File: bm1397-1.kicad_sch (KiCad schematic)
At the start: 58 parts, among them IC1 BM1397_mode1, J8 Conn_01x05, U5 MCP1824T-1802E, U6 MCP1824T-0802E, X1 OT322525MJBA4SL

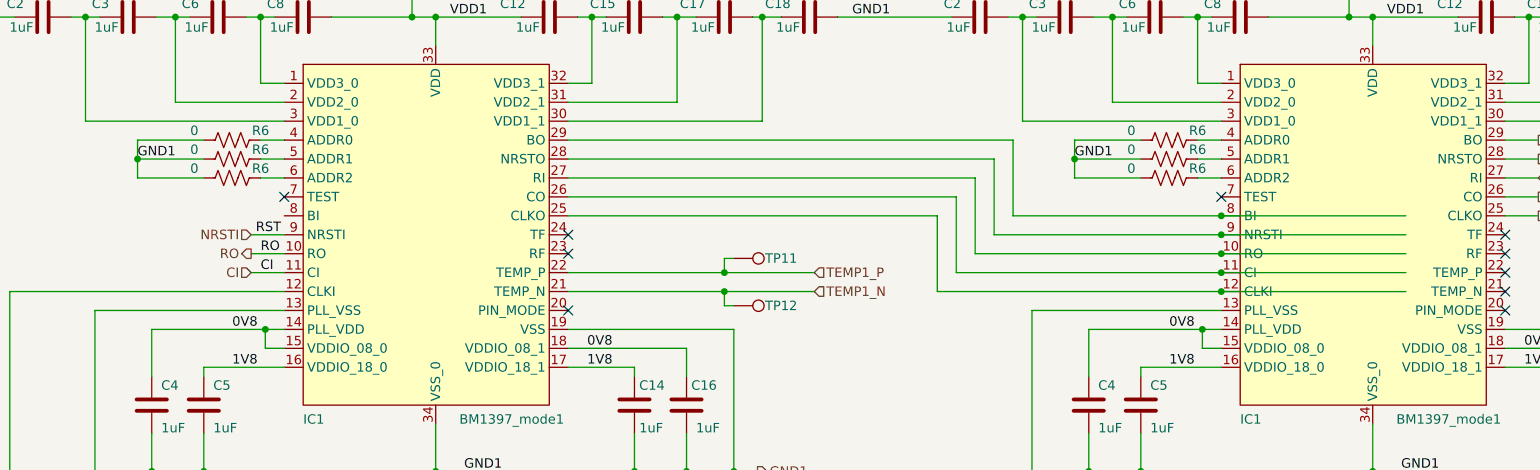
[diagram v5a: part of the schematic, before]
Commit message: add 10k pull-down on first BM1397 BI signal
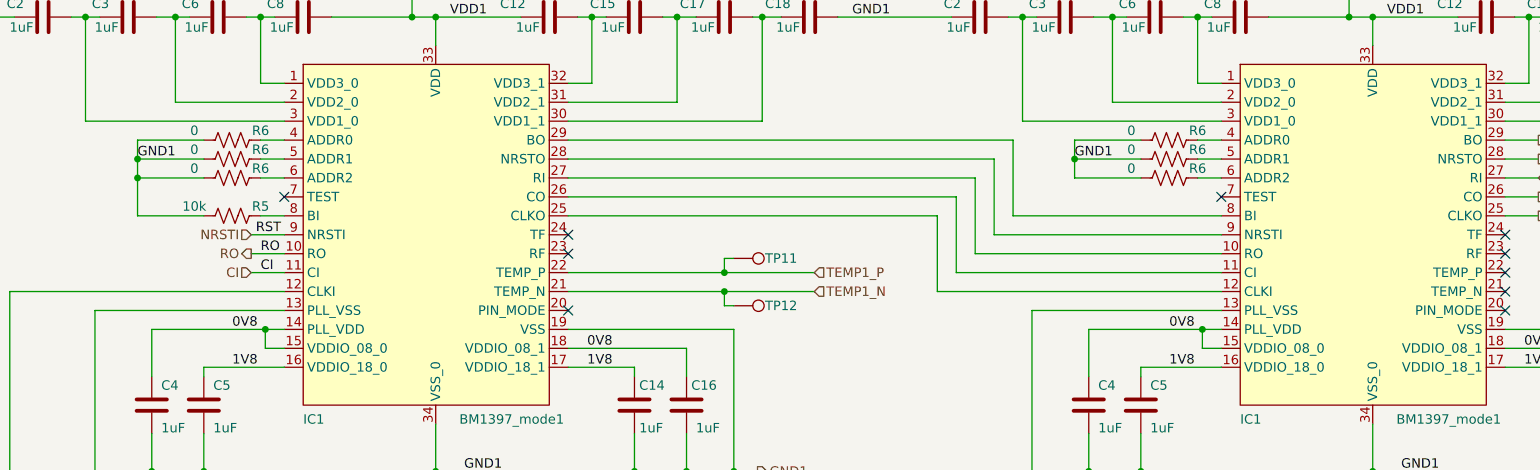
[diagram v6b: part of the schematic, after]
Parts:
- added R5: 10k, Resistor_SMD:R_0402_1005Metric, symbol Device:R_US
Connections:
- net GND1: now also R5.1
- net at IC1.8 (BI): now also R5.2
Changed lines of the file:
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@@
   (junction (at 205.74 105.41) (diameter 0) (color 0 0 0 0)
   )
+  (junction (at 40.005 66.04) (diameter 0) (color 0 0 0 0)
+  )
   (junction (at 165.735 63.5) (diameter 0) (color 0 0 0 0)
   )
@@
   (junction (at 76.835 163.83) (diameter 0.9144) (color 0 0 0 0)
   )
-  (junction (at 185.42 78.74) (diameter 0) (color 0 0 0 0)
-  )
   (junction (at 118.745 81.28) (diameter 0) (color 0 0 0 0)
   )
@@
   (junction (at 120.015 105.41) (diameter 0) (color 0 0 0 0)
   )
-  (junction (at 185.42 76.2) (diameter 0) (color 0 0 0 0)
-  )
   (junction (at 57.15 86.36) (diameter 0) (color 0 0 0 0)
   )
@@
   (junction (at 213.36 29.845) (diameter 0) (color 0 0 0 0)
   )
-  (junction (at 185.42 73.66) (diameter 0) (color 0 0 0 0)
-  )
   (junction (at 100.965 44.45) (diameter 0) (color 0 0 0 0)
   )
@@
   (junction (at 193.04 17.145) (diameter 0.9144) (color 0 0 0 0)
   )
-  (junction (at 185.42 71.12) (diameter 0) (color 0 0 0 0)
-  )
   (junction (at 182.245 44.45) (diameter 0) (color 0 0 0 0)
   )
   (junction (at 67.31 17.145) (diameter 0.9144) (color 0 0 0 0)
   )
-  (junction (at 185.42 81.28) (diameter 0) (color 0 0 0 0)
-  )
   (junction (at 106.68 105.41) (diameter 0) (color 0 0 0 0)
   )
@@
     (stroke (width 0) (type default))
   )
-  (wire (pts (xy 185.42 76.2) (xy 210.185 76.2))
-    (stroke (width 0) (type default))
-  )
   (wire (pts (xy 100.965 44.45) (xy 102.87 44.45))
     (stroke (width 0) (type default))
@@
     (stroke (width 0) (type solid))
   )
+  (wire (pts (xy 48.895 71.12) (xy 40.005 71.12))
+    (stroke (width 0) (type default))
+  )
   (wire (pts (xy 167.64 92.71) (xy 167.64 86.36))
     (stroke (width 0) (type default))
@@
     (stroke (width 0) (type default))
   )
-  (wire (pts (xy 185.42 73.66) (xy 210.185 73.66))
-    (stroke (width 0) (type default))
-  )
   (wire (pts (xy 158.75 44.45) (xy 160.655 44.45))
     (stroke (width 0) (type default))
@@
     (stroke (width 0) (type default))
   )
-  (wire (pts (xy 34.29 83.82) (xy 34.29 105.41))
+  (wire (pts (xy 40.005 71.12) (xy 40.005 66.04))
     (stroke (width 0) (type default))
   )
-  (wire (pts (xy 48.895 105.41) (xy 80.01 105.41))
+  (wire (pts (xy 34.29 83.82) (xy 34.29 105.41))
     (stroke (width 0) (type default))
   )
-  (wire (pts (xy 185.42 71.12) (xy 210.185 71.12))
+  (wire (pts (xy 48.895 105.41) (xy 80.01 105.41))
     (stroke (width 0) (type default))
   )
@@
     (stroke (width 0) (type default))
   )
-  (wire (pts (xy 185.42 78.74) (xy 210.185 78.74))
-    (stroke (width 0) (type default))
-  )
   (wire (pts (xy 97.79 53.34) (xy 100.965 53.34))
     (stroke (width 0) (type default))
@@
     (stroke (width 0) (type solid))
   )
-  (wire (pts (xy 185.42 81.28) (xy 210.185 81.28))
-    (stroke (width 0) (type default))
-  )
   (wire (pts (xy 149.86 68.58) (xy 149.86 78.74))
     (stroke (width 0) (type default))
@@
     (stroke (width 0) (type default))
   )
+  (wire (pts (xy 56.515 71.12) (xy 59.69 71.12))
+    (stroke (width 0) (type default))
+  )
   (wire (pts (xy 193.04 17.145) (xy 203.2 17.145))
     (stroke (width 0) (type solid))
@@
         )
       )
+    )
+  )
+  (symbol (lib_id "Device:R_US") (at 52.705 71.12 90) (unit 1)
+    (in_bom yes) (on_board yes) (dnp no)
+    (property "Reference" "R5" (at 56.515 69.85 90)
+      (effects (font (size 1.27 1.27)))
+    )
+    (property "Value" "10k" (at 47.625 69.85 90)
+      (effects (font (size 1.27 1.27)))
+    )
+    (property "Footprint" "Resistor_SMD:R_0402_1005Metric" (at 52.959 70.104 90)
+      (effects (font (size 1.27 1.27)) hide)
+    )
+    (property "Datasheet" "~" (at 52.705 71.12 0)
+      (effects (font (size 1.27 1.27)) hide)
+    )
+    (property "DK" "311-10KJRCT-ND" (at 52.705 71.12 0)
+      (effects (font (size 1.27 1.27)) hide)
+    )
+    (property "PARTNO" "RC0402JR-0710KL" (at 52.705 71.12 0)
+      (effects (font (size 1.27 1.27)) hide)
+    )
+    (pin "1")
+    (pin "2")
+    (instances
+      (project "bitaxeHex"
+        (path "/e63e39d7-6ac0-4ffd-8aa3-1841a4541b55/8ec0a9c6-2b78-44ef-a83d-9047d2828409"
+          (reference "R5") (unit 1)
+        )
+        (path "/e63e39d7-6ac0-4ffd-8aa3-1841a4541b55/4cf9c075-d009-4c35-9949-adda70ae20c7"
+          (reference "R43") (unit 1)
+        )
+      )
